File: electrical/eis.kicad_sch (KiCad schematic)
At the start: 51 parts

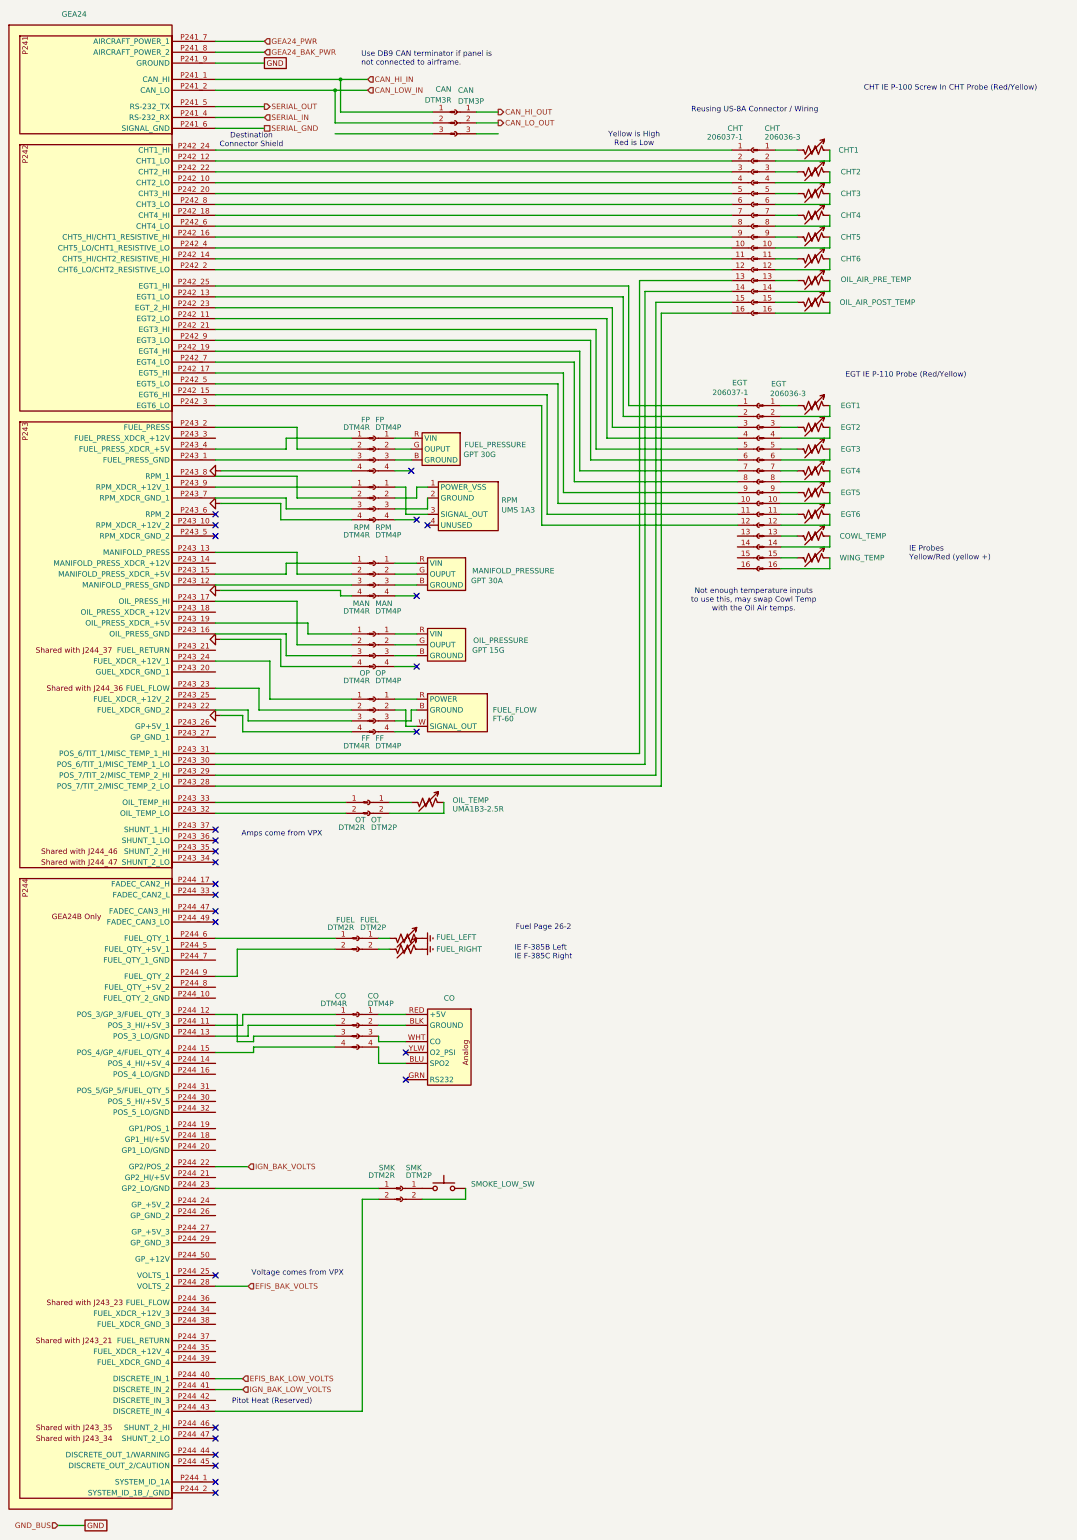
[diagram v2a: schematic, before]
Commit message: Interim check-in getting colors correct.
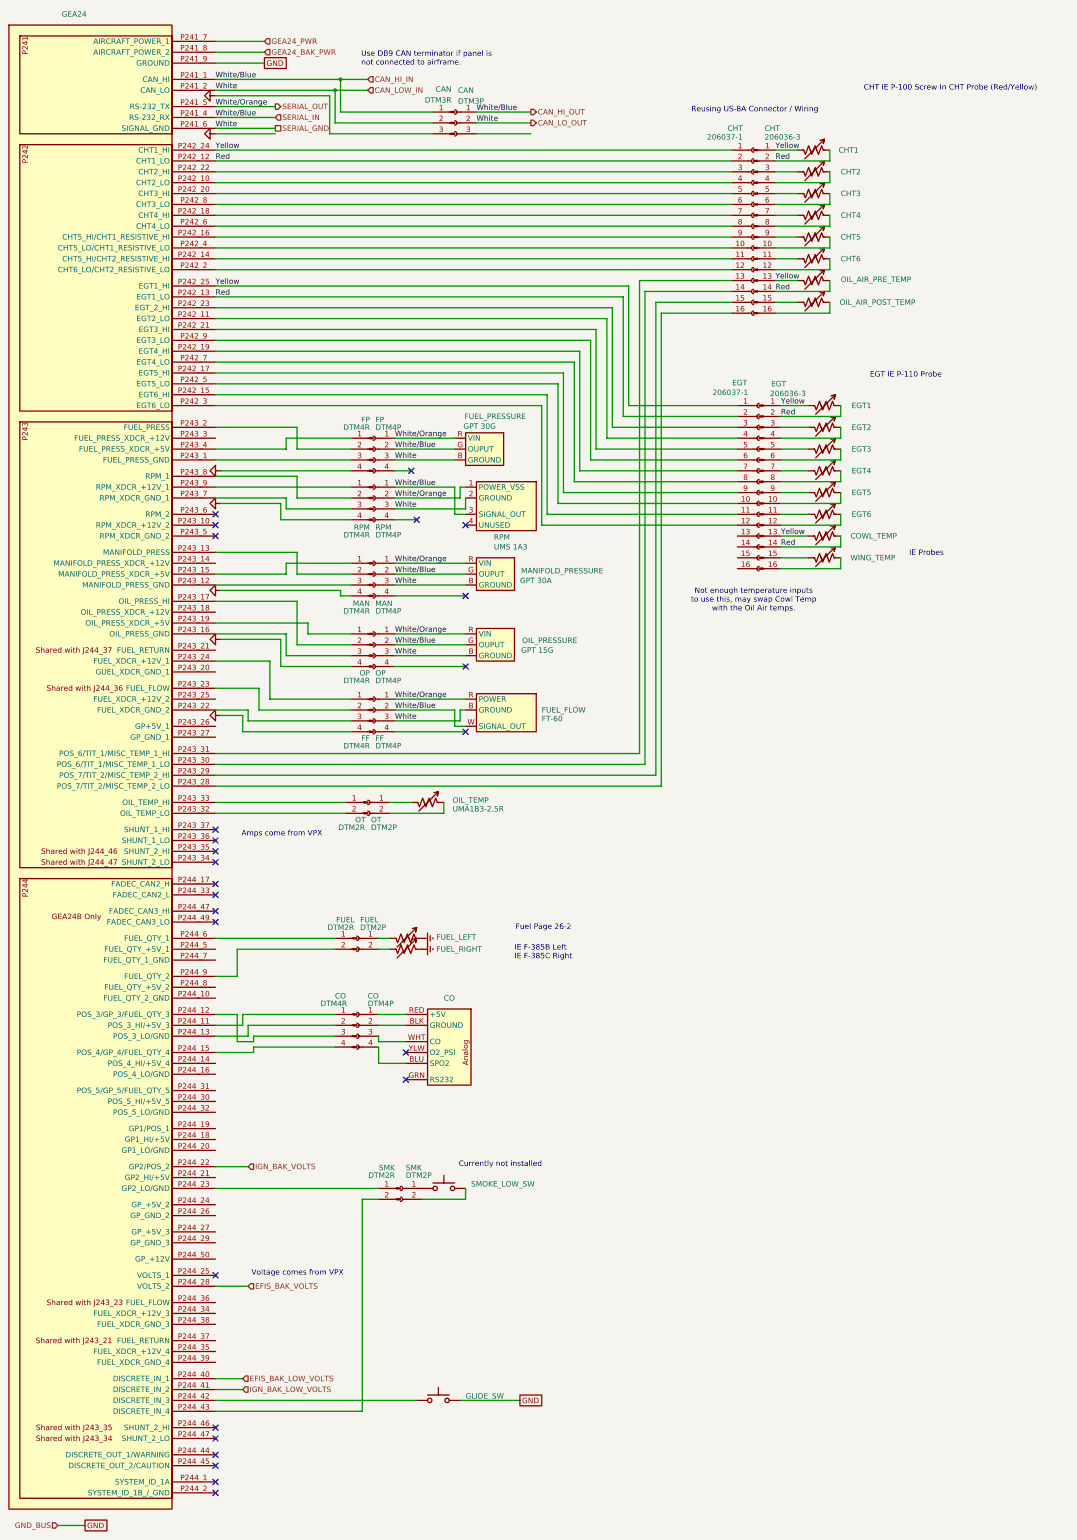
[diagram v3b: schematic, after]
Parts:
- added GLIDE_SW: FLOAT_SENSOR, symbol Switch:SW_Push
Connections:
- net CAN_HI_OUT is gone; now on net CAN_HI_IN: CAN.1 (Pin_1)
- net CAN_LO_OUT is gone; now on net CAN_LOW_IN: CAN.2 (Pin_2)
- net SERIAL_GND is gone; now on net CAN_LOW_IN: GEA24.P241_6 (SIGNAL_GND)
- net SERIAL_IN is gone; now on net CAN_HI_IN: GEA24.P241_4 (RS-232_RX)
- net CAN_HI_IN: now also FF.2 (Pin_2), FP.2 (Pin_2), FUEL_FLOW.W (SIGNAL_OUT), FUEL_PRESSURE.G (OUPUT), MAN.2 (Pin_2), MANIFOLD_PRESSURE.G (OUPUT), OIL_PRESSURE.G (OUPUT), OP.2 (Pin_2), RPM.1 (Pin_1), RPM.3 (SIGNAL_OUT)
- net CAN_LOW_IN: now also FF.3 (Pin_3), FP.3 (Pin_3), FUEL_FLOW.B (GROUND), FUEL_PRESSURE.B (GROUND), MAN.3 (Pin_3), MANIFOLD_PRESSURE.B (GROUND), OIL_PRESSURE.B (GROUND), OP.3 (Pin_3), RPM.2 (GROUND), RPM.3 (Pin_3)
- net GND: now also GLIDE_SW.2
- net GNDS: now also CAN.3 (Pin_3)
- net SERIAL_OUT: now also FF.1 (Pin_1), FP.1 (Pin_1), FUEL_FLOW.R (POWER), FUEL_PRESSURE.R (VIN), MAN.1 (Pin_1), MANIFOLD_PRESSURE.R (VIN), OIL_PRESSURE.R (VIN), OP.1 (Pin_1), RPM.1 (POWER_VSS), RPM.2 (Pin_2)
- net Red: now reaches CHT.14 (Pin_14), OIL_AIR_PRE_TEMP.1
- net Red: now also CHT.2 (Pin_2), CHT.2 (Pin_2), CHT1.1, COWL_TEMP.1, EGT.14 (Pin_14), EGT.2 (Pin_2), EGT.2 (Pin_2), EGT1.1, GEA24.P242_12 (CHT1_LO), GEA24.P242_13 (EGT1_LO)
- net Yellow: now reaches CHT.13 (Pin_13), OIL_AIR_PRE_TEMP.2
- net Yellow: now also CHT.1 (Pin_1), CHT.1 (Pin_1), CHT1.2, COWL_TEMP.2, EGT.1 (Pin_1), EGT.1 (Pin_1), EGT.13 (Pin_13), EGT1.2, GEA24.P242_24 (CHT1_HI), GEA24.P242_25 (EGT1_HI)
- net at GEA24.P244_42 (DISCRETE_IN_3): now also GLIDE_SW.1
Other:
- note added: "Currently not installed"
- note added: "EGT IE P-110 Probe"
- note added: "IE Probes"
- note removed: "Destination Connector Shield"
- note removed: "EGT IE P-110 Probe (Red/Yellow)"
- note removed: "IE Probes Yellow/Red (yellow +)"
- note removed: "Pitot Heat (Reserved)"
- note removed: "Yellow is High Red is Low"
- moved on the sheet: COWL_TEMP, EGT1, EGT2, EGT3, EGT4, EGT5, EGT6, FUEL_FLOW, FUEL_PRESSURE, MANIFOLD_PRESSURE, OIL_PRESSURE, RPM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

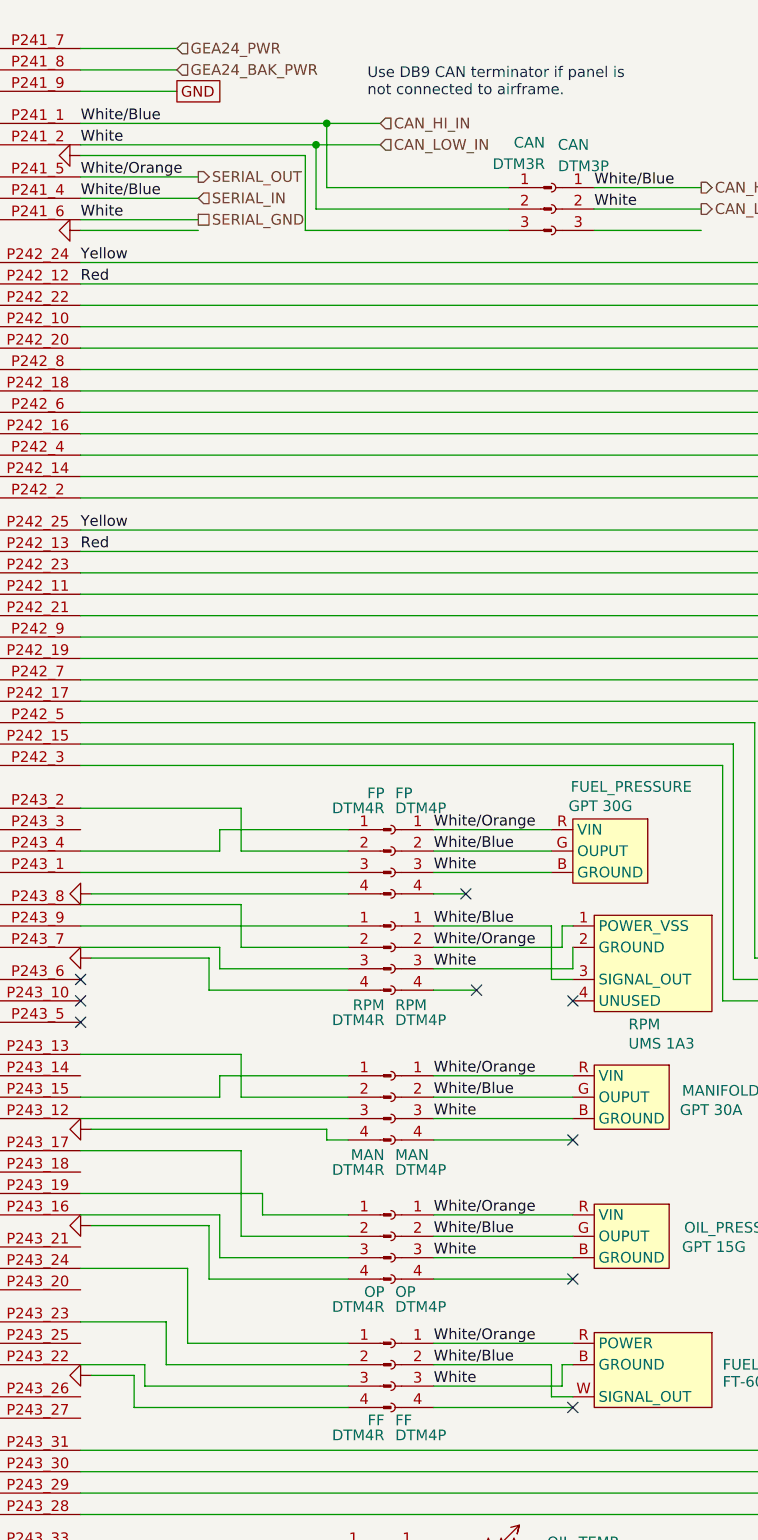
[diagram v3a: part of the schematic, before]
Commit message: Added shielding and wire colors and corrections.
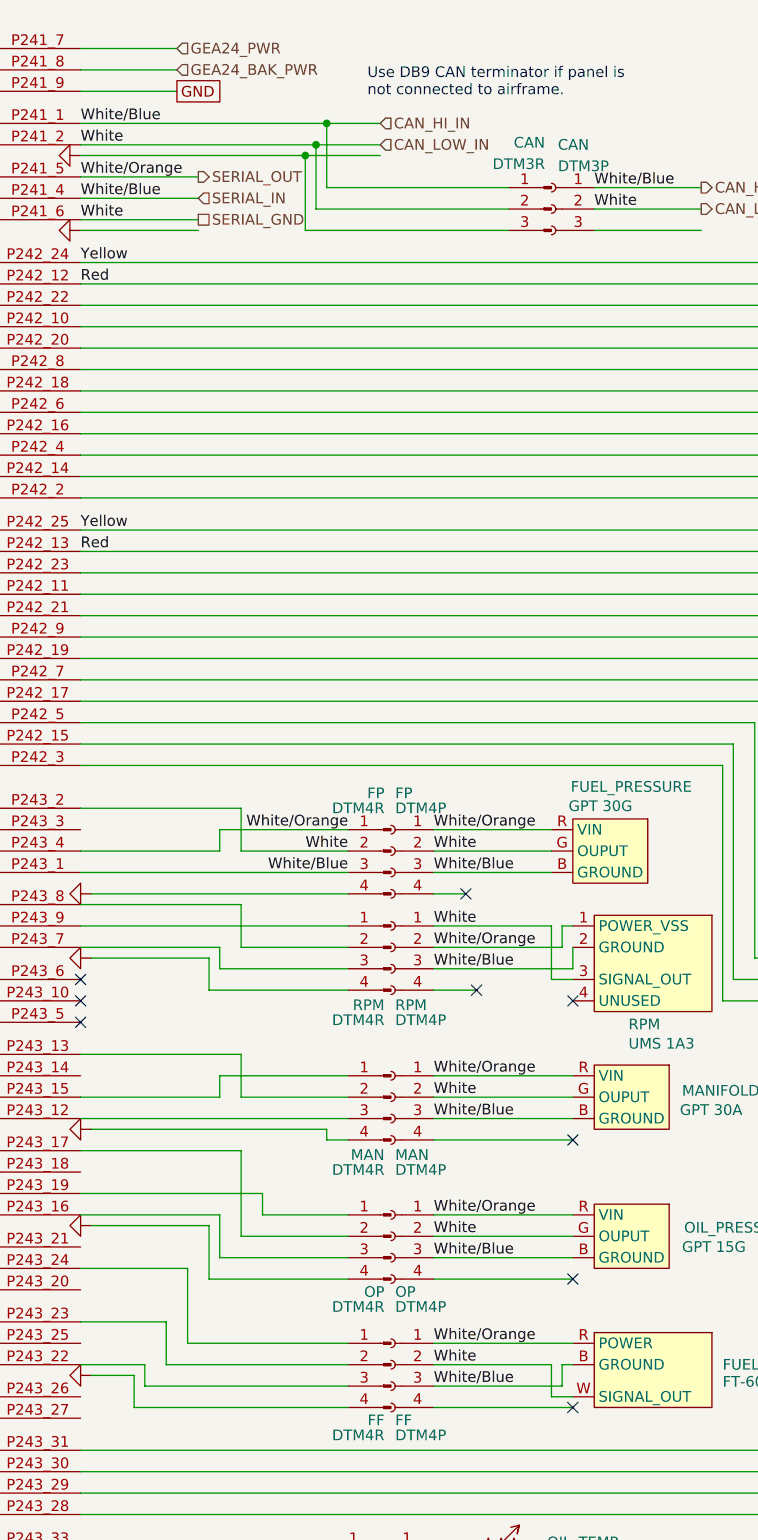
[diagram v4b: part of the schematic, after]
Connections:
- net CAN_HI_IN: now also FF.3 (Pin_3), FP.3 (Pin_3), FP.3 (Pin_3), FUEL_FLOW.B (GROUND), FUEL_PRESSURE.B (GROUND), GEA24.P243_1 (FUEL_PRESS_GND), MAN.3 (Pin_3), MANIFOLD_PRESSURE.B (GROUND), OIL_PRESSURE.B (GROUND), OP.3 (Pin_3), RPM.2 (GROUND), RPM.3 (Pin_3); no longer FF.2 (Pin_2), FP.2 (Pin_2), FUEL_FLOW.W (SIGNAL_OUT), FUEL_PRESSURE.G (OUPUT), MAN.2 (Pin_2), MANIFOLD_PRESSURE.G (OUPUT), OIL_PRESSURE.G (OUPUT), OP.2 (Pin_2), RPM.1 (Pin_1), RPM.3 (SIGNAL_OUT)
- net CAN_LOW_IN: now also FF.2 (Pin_2), FP.2 (Pin_2), FP.2 (Pin_2), FUEL_FLOW.W (SIGNAL_OUT), FUEL_PRESSURE.G (OUPUT), GEA24.P243_2 (FUEL_PRESS), MAN.2 (Pin_2), MANIFOLD_PRESSURE.G (OUPUT), OIL_PRESSURE.G (OUPUT), OP.2 (Pin_2), RPM.1 (Pin_1), RPM.3 (SIGNAL_OUT); no longer FF.3 (Pin_3), FP.3 (Pin_3), FUEL_FLOW.B (GROUND), FUEL_PRESSURE.B (GROUND), MAN.3 (Pin_3), MANIFOLD_PRESSURE.B (GROUND), OIL_PRESSURE.B (GROUND), OP.3 (Pin_3), RPM.2 (GROUND), RPM.3 (Pin_3)
- net SERIAL_OUT: now also FP.1 (Pin_1), GEA24.P243_4 (FUEL_PRESS_XDCR_+5V)
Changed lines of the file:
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@@
 	(title_block
 		(title "EIS")
-		(date "2025-11-03")
-		(rev "1.2.2")
+		(date "2025-11-12")
+		(rev "1.2.5")
 		(company "N78HR")
 	)
@@
 		(color 0 0 0 0)
 	)
+	(junction
+		(at 93.98 34.29)
+		(diameter 0)
+		(color 0 0 0 0)
+	)
 	(no_connect
 		(at 67.31 227.33)
@@
 	(wire
 		(pts
+			(xy 93.98 34.29) (xy 102.87 34.29)
+		)
+		(stroke
+			(width 0)
+			(type dash)
+		)
+	)
+	(wire
+		(pts
 			(xy 67.31 166.37) (xy 80.01 166.37)
 		)
@@
 		)
 	)
-	(label "White{slash}Blue"
+	(label "White"
 		(at 109.22 162.56 0)
 		(effects
@@
 		)
 	)
-	(label "White"
+	(label "White{slash}Blue"
 		(at 109.22 165.1 0)
 		(effects
@@
 		)
 	)
+	(label "White"
+		(at 109.22 125.73 0)
+		(effects
+			(font
+				(size 1.27 1.27)
+			)
+			(justify left bottom)
+		)
+	)
 	(label "White{slash}Blue"
-		(at 109.22 125.73 0)
-		(effects
-			(font
-				(size 1.27 1.27)
-			)
-			(justify left bottom)
-		)
-	)
-	(label "White"
 		(at 109.22 119.38 0)
 		(effects
@@
 			)
 			(justify left bottom)
+		)
+	)
+	(label "White{slash}Orange"
+		(at 99.06 114.3 180)
+		(effects
+			(font
+				(size 1.27 1.27)
+			)
+			(justify right bottom)
 		)
 	)
@@
 		)
 	)
+	(label "White{slash}Blue"
+		(at 109.22 130.81 0)
+		(effects
+			(font
+				(size 1.27 1.27)
+			)
+			(justify left bottom)
+		)
+	)
 	(label "White"
-		(at 109.22 130.81 0)
-		(effects
-			(font
-				(size 1.27 1.27)
-			)
-			(justify left bottom)
+		(at 99.06 116.84 180)
+		(effects
+			(font
+				(size 1.27 1.27)
+			)
+			(justify right bottom)
 		)
 	)
@@
 		)
 	)
-	(label "White{slash}Blue"
+	(label "White"
 		(at 109.22 146.05 0)
 		(effects
@@
 		)
 	)
-	(label "White"
+	(label "White{slash}Blue"
 		(at 109.22 148.59 0)
 		(effects
@@
 		)
 	)
+	(label "White{slash}Blue"
+		(at 99.06 119.38 180)
+		(effects
+			(font
+				(size 1.27 1.27)
+			)
+			(justify right bottom)
+		)
+	)
 	(label "White{slash}Orange"
 		(at 109.22 143.51 0)
@@
 		)
 	)
+	(label "White"
+		(at 109.22 116.84 0)
+		(effects
+			(font
+				(size 1.27 1.27)
+			)
+			(justify left bottom)
+		)
+	)
+	(label "White"
+		(at 109.22 177.8 0)
+		(effects
+			(font
+				(size 1.27 1.27)
+			)
+			(justify left bottom)
+		)
+	)
 	(label "White{slash}Blue"
-		(at 109.22 116.84 0)
-		(effects
-			(font
-				(size 1.27 1.27)
-			)
-			(justify left bottom)
-		)
-	)
-	(label "White{slash}Blue"
-		(at 109.22 177.8 0)
-		(effects
-			(font
-				(size 1.27 1.27)
-			)
-			(justify left bottom)
-		)
-	)
-	(label "White"
 		(at 109.22 180.34 0)
 		(effects

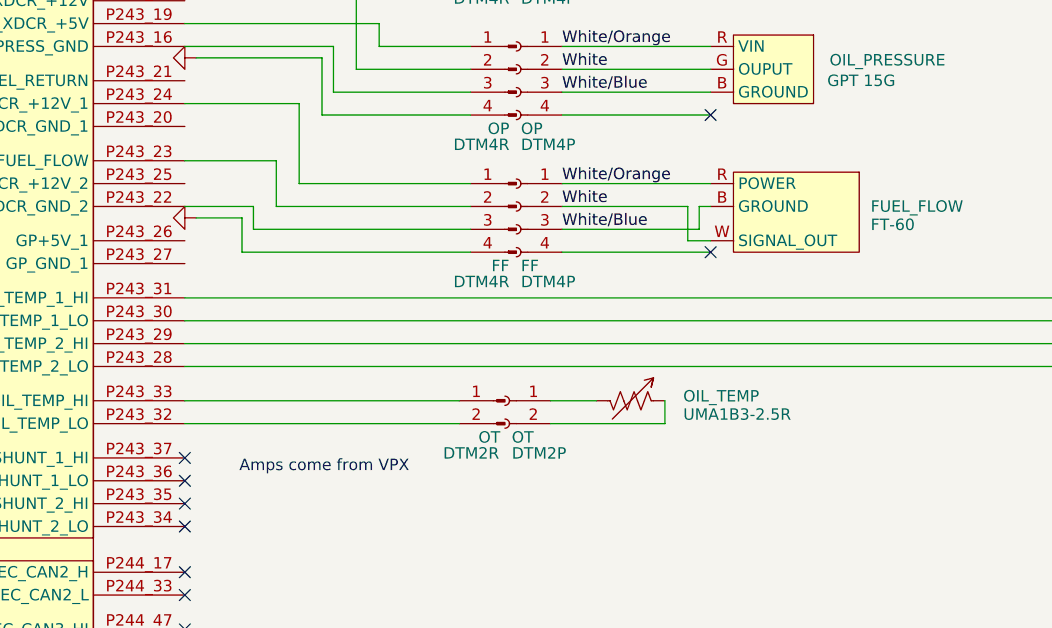
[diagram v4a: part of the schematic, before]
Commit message: Changed Oil Temp to shielded. Added colors that matched what wired.
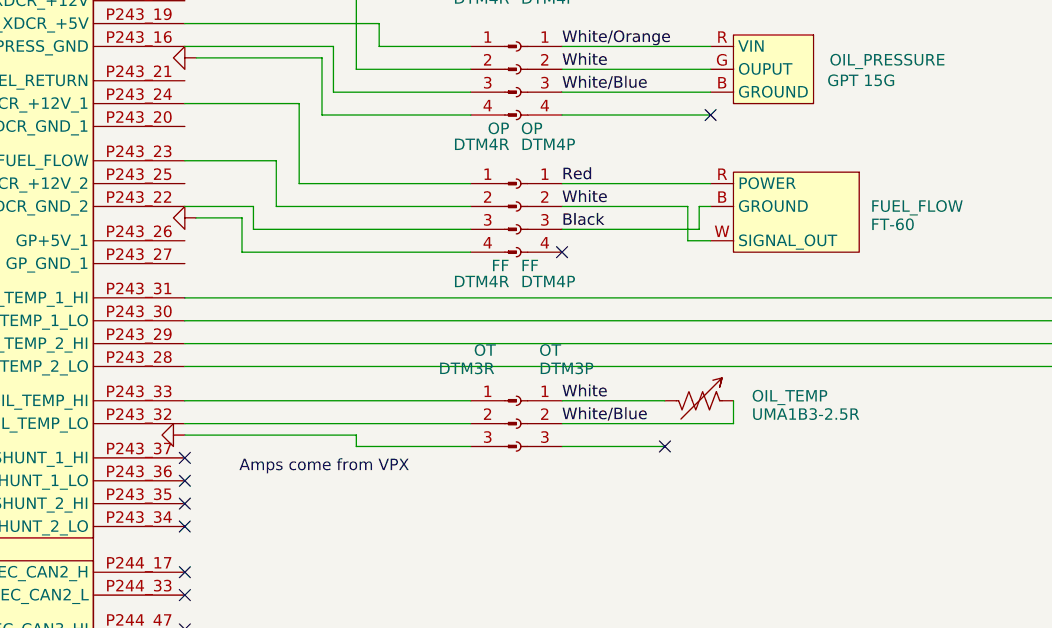
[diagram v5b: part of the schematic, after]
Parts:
- removed OT: DTM2P, symbol Connector:Conn_01x02_Socket
- removed OT: DTM2R, symbol Connector:Conn_01x02_Pin
- added OT: DTM3R, symbol Connector:Conn_01x03_Pin
- added OT: DTM3P, symbol Connector:Conn_01x03_Socket
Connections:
- net CAN_HI_IN: now also OIL_TEMP.1, OT.2 (Pin_2); no longer FF.3 (Pin_3), FUEL_FLOW.B (GROUND)
- net CAN_LOW_IN: now also OIL_TEMP.2, OT.1 (Pin_1)
- net GNDS: now also OT.3 (Pin_3)
- net Red: now also FF.1 (Pin_1), FUEL_FLOW.R (POWER)
- net SERIAL_OUT: no longer FF.1 (Pin_1), FUEL_FLOW.R (POWER)
- net at GEA24.P243_32 (OIL_TEMP_LO): now also OT.2 (Pin_2)
- net at GEA24.P243_33 (OIL_TEMP_HI): now also OT.1 (Pin_1)
- new net Black: FF.3 (Pin_3), FUEL_FLOW.B (GROUND)
- no-connect marks 26 -> 27
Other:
- moved on the sheet: OIL_TEMP
